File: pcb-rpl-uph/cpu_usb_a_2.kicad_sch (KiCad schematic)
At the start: 1 part, among them U5 RPL_UPH_FCBGA1744

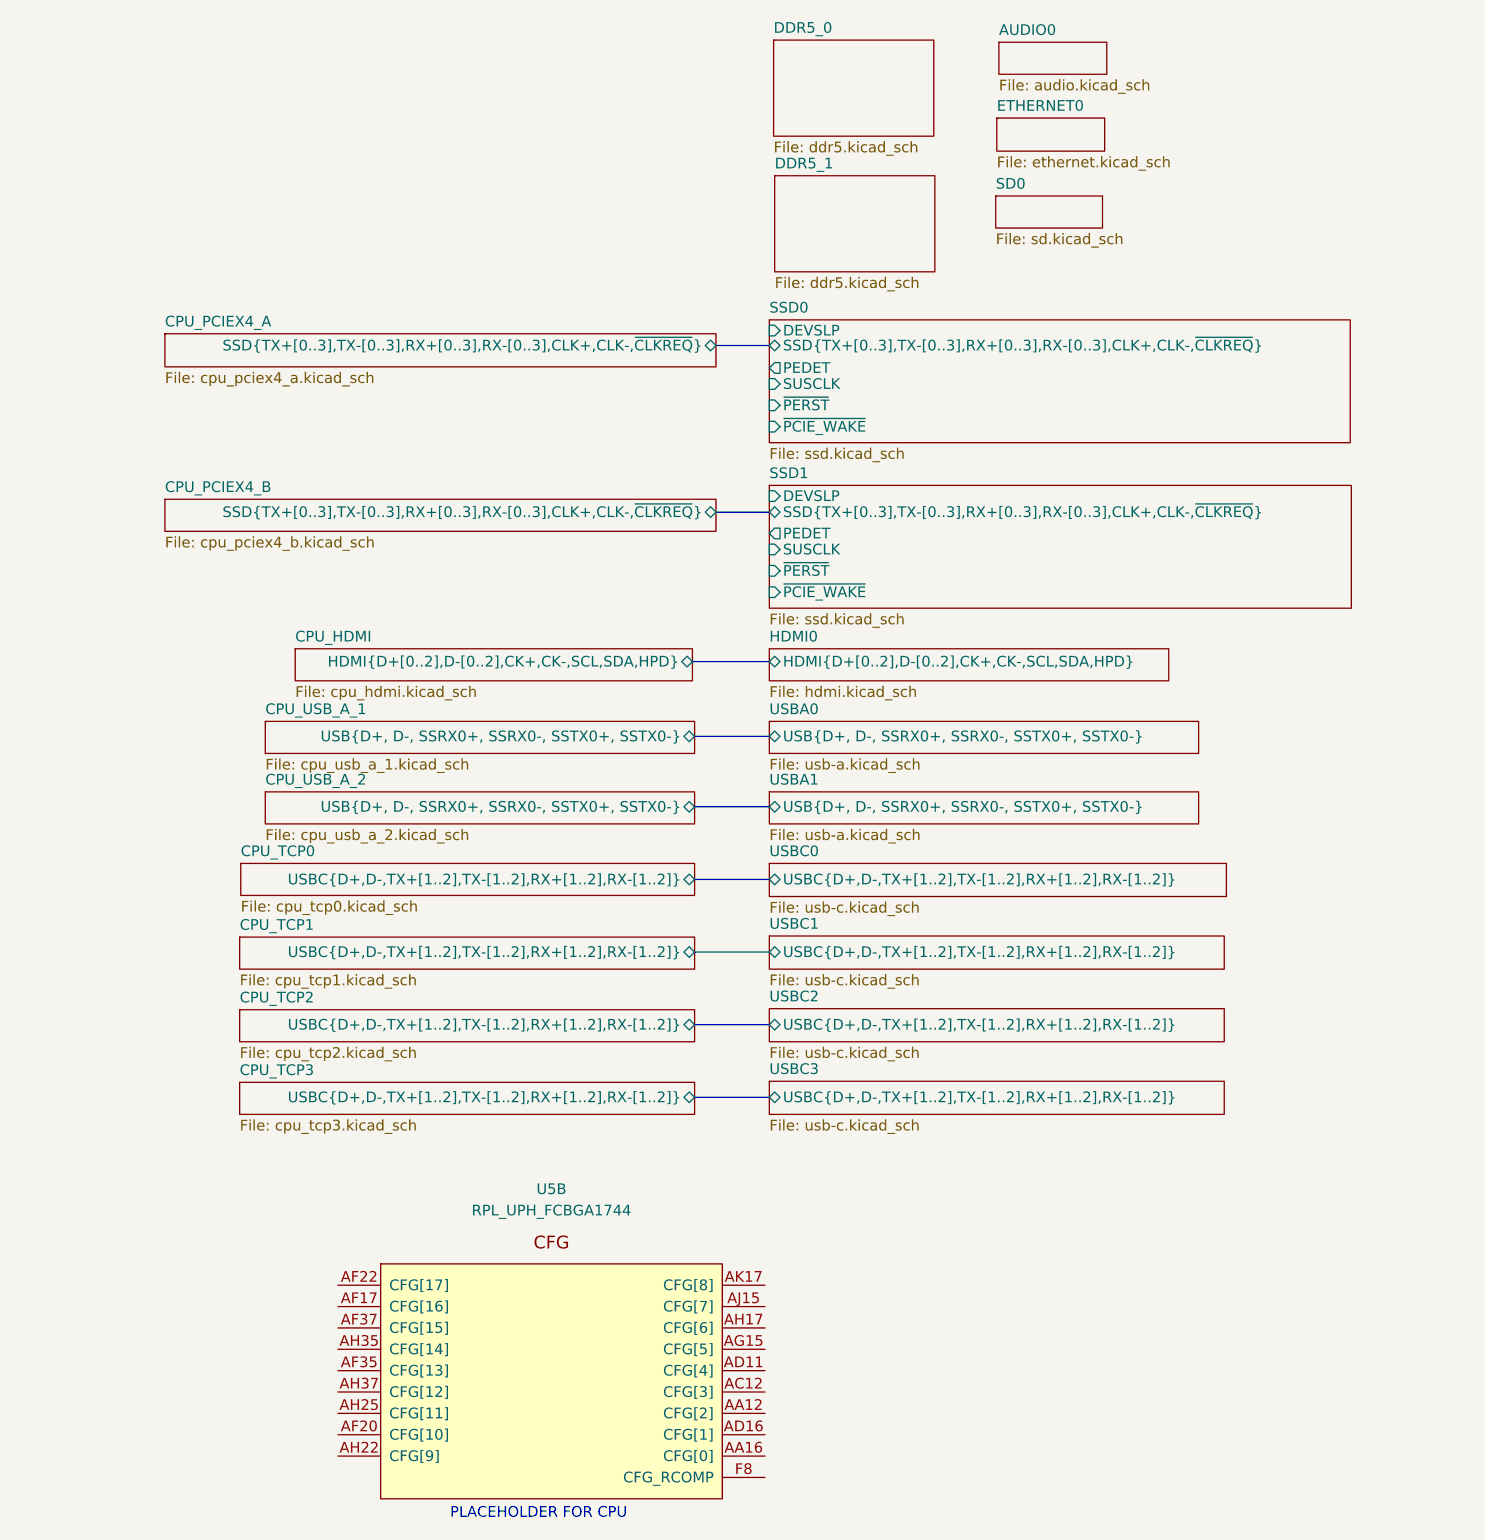
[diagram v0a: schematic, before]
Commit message: Connect USB-A and USB-C data
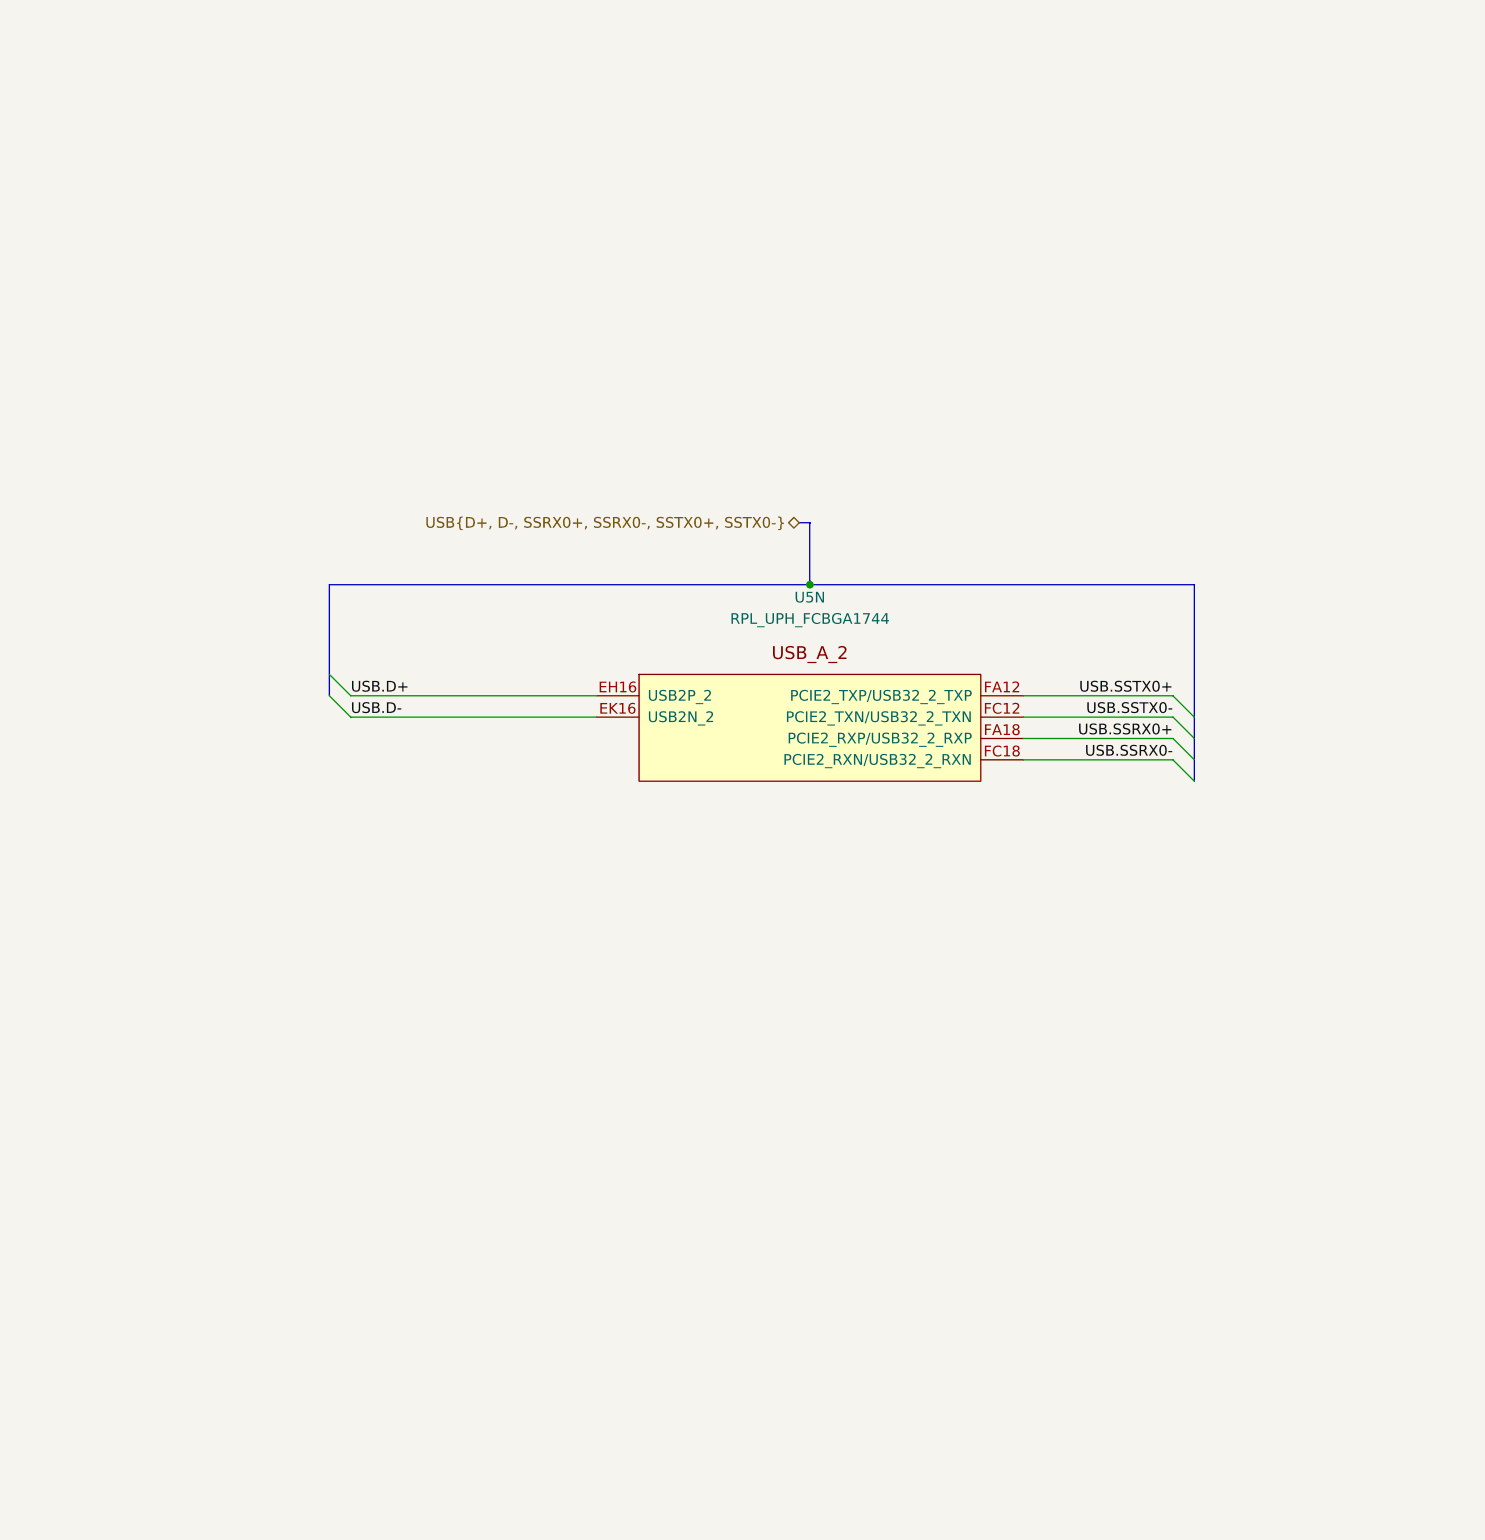
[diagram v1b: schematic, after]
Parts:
- removed U5: RPL_UPH_FCBGA1744, local:RPL_UPH_FCBGA1744, symbol local:RPL_UPH_FCBGA1744
- added U5: RPL_UPH_FCBGA1744, symbol local:RPL_UPH_FCBGA1744
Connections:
- new net USB.D+: U5.EH16 (USB2P_2)
- new net USB.D-: U5.EK16 (USB2N_2)
- new net USB.SSRX0+: U5.FA18 (PCIE2_RXP/USB32_2_RXP)
- new net USB.SSRX0-: U5.FC18 (PCIE2_RXN/USB32_2_RXN)
- new net USB.SSTX0+: U5.FA12 (PCIE2_TXP/USB32_2_TXP)
- new net USB.SSTX0-: U5.FC12 (PCIE2_TXN/USB32_2_TXN)
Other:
- removed sheet AUDIO0
- removed sheet CPU_HDMI
- removed sheet CPU_PCIEX4_A
- removed sheet CPU_PCIEX4_B
- removed sheet CPU_TCP0
- removed sheet CPU_TCP1
- removed sheet CPU_TCP2
- removed sheet CPU_TCP3
- removed sheet CPU_USB_A_1
- removed sheet CPU_USB_A_2
- removed sheet DDR5_0
- removed sheet DDR5_1
- removed sheet ETHERNET0
- removed sheet HDMI0
- removed sheet SD0
- removed sheet SSD0
- removed sheet SSD1
- removed sheet USBA0
- removed sheet USBA1
- removed sheet USBC0
- removed sheet USBC1
- removed sheet USBC2
- removed sheet USBC3
- note removed: "PLACEHOLDER FOR CPU"

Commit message: add display connector
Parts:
- U5: footprint (none) -> local:RPL_UPH_FCBGA1744
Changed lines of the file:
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@@
       (effects (font (size 1.27 1.27)))
     )
-    (property "Footprint" "" (at 147.066 87.884 0)
+    (property "Footprint" "local:RPL_UPH_FCBGA1744" (at 147.066 87.884 0)
       (effects (font (size 1.27 1.27)) hide)
     )
